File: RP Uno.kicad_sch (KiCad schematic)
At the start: 58 parts, among them J1 USB_B, J2 Conn_01x08, J3 Conn_01x06, J4 Conn_01x10, J5 Conn_01x08, J6 Barrel_Jack_Switch, J7 ICSP, J8 SWD, Q1 FDN340P, Q2 FDN340P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

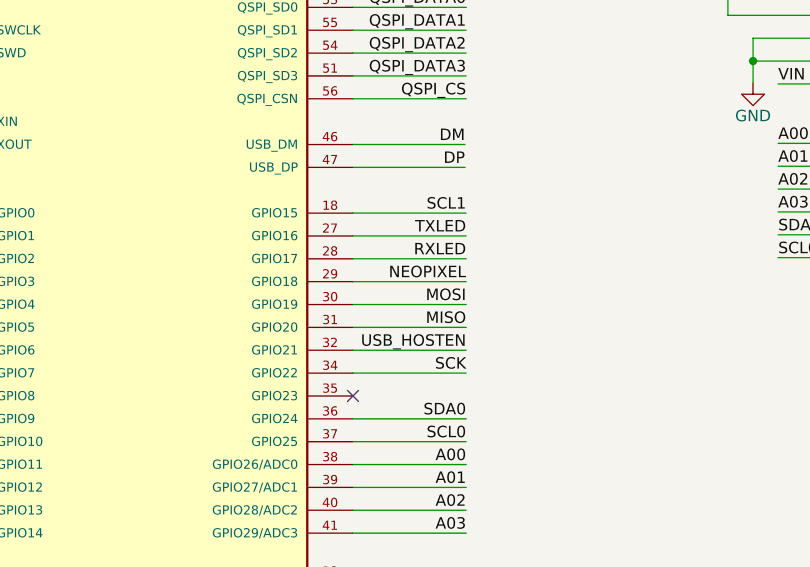
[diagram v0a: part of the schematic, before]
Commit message: Pinout changes and silkscreen additions
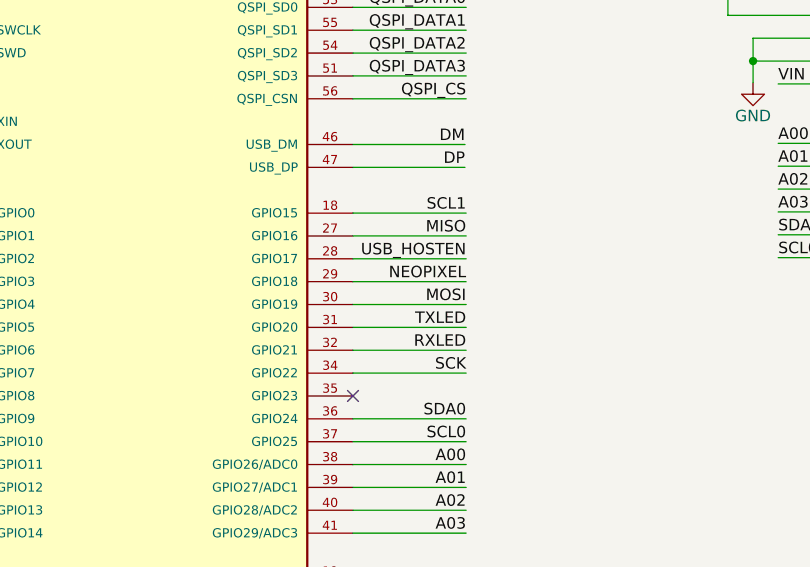
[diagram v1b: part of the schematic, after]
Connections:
- net MISO: now also U1.27 (GPIO16); no longer U1.31 (GPIO20)
- net RXLED: now also U1.32 (GPIO21); no longer U1.28 (GPIO17)
- net TXLED: now also U1.31 (GPIO20); no longer U1.27 (GPIO16)
- net USB_HOSTEN: now also U1.28 (GPIO17); no longer U1.32 (GPIO21)
